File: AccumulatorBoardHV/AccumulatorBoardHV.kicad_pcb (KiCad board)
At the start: 2 copper layers, 179.7 x 69.2 mm, 48 parts, among them J1 TS -> GLV Regulator Jumper, J10 Charger Current, J2 To LV Board, J3 Batt Voltage, J4 TS (Switched), J5 IMD TS, J6 To LV Board, J7 Acc LED 1, J8 Acc LED 2, J9 Charger Current to Batt, U1 V110C12E100BL, U2 DK1A1B-12V, U3 RDD08110S3V3, U4 PS2501-4, U5 G2RL-1A-E, U6 G2RL-1A-E

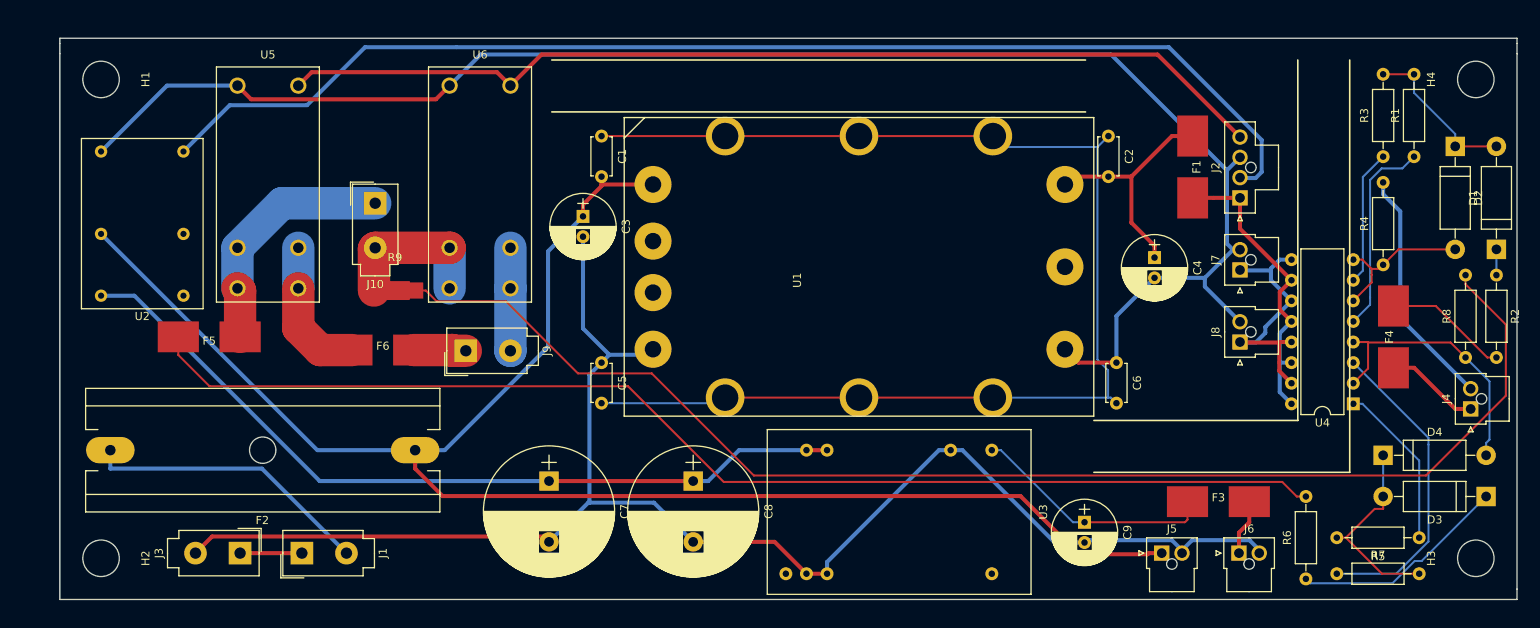
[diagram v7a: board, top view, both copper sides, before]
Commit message: Tweak silkscreen labels on boards for final run
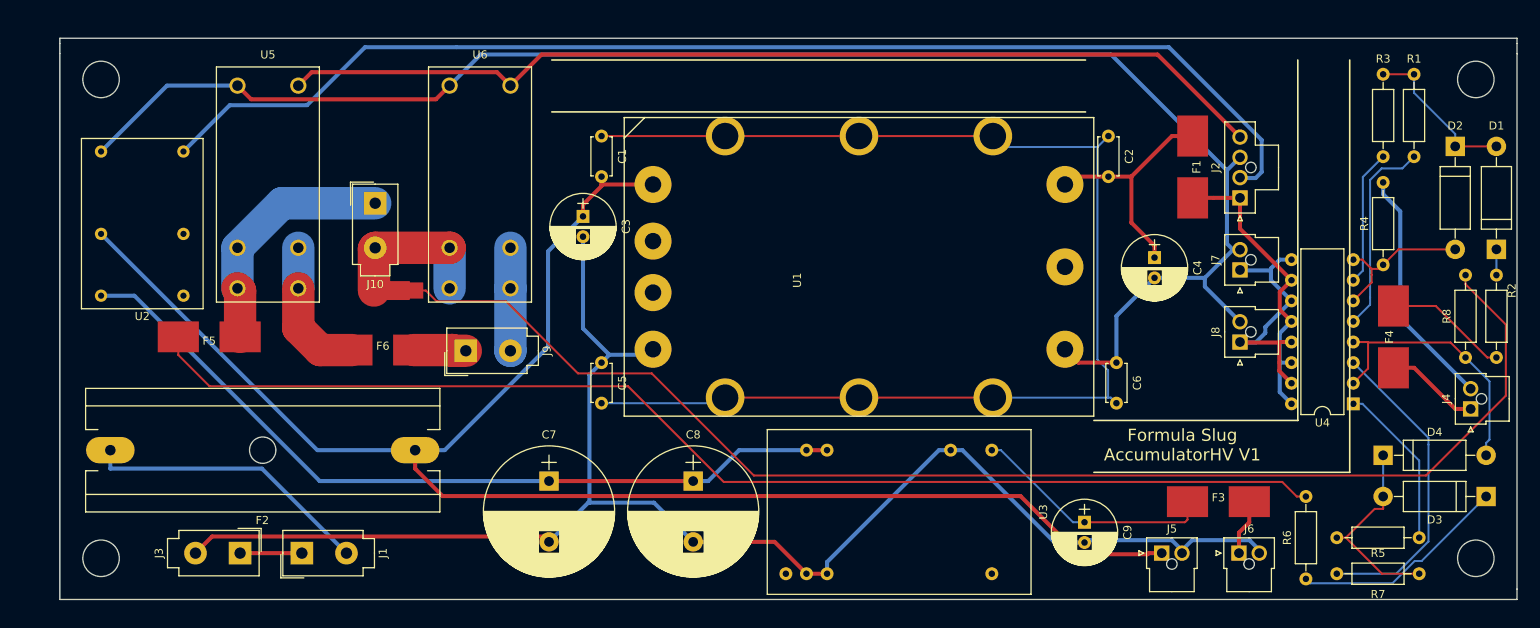
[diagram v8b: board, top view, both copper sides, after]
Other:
- board text added: "Formula Slug AccumulatorHV V1"
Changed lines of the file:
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@@
     (area 21.9 31.019999 204.895 106.253097)
     (thickness 1.6)
-    (drawings 15)
+    (drawings 16)
     (tracks 264)
     (zones 0)
@@
     (descr "Just a \"Net tie\" as an more or less elegant way to connect two different nets without disturbing ERC and DRC.")
     (tags "Just a \"Net tie\" as an more or less elegant way to connect two different nets without disturbing ERC and DRC.")
-    (fp_text reference R9 (at -0.04064 4.06908 180) (layer F.SilkS)
+    (fp_text reference R9 (at 0 -1.905 180) (layer F.SilkS) hide
       (effects (font (size 1 1) (thickness 0.15)))
     )
@@
     (tags "mounting hole 4.5mm no annular")
     (attr virtual)
-    (fp_text reference H4 (at 0 -5.5 90) (layer F.SilkS)
+    (fp_text reference H4 (at 0 -5.5 90) (layer F.SilkS) hide
       (effects (font (size 1 1) (thickness 0.15)))
     )
@@
     (tags "mounting hole 4.5mm no annular")
     (attr virtual)
-    (fp_text reference H3 (at 0 -5.5 90) (layer F.SilkS)
+    (fp_text reference H3 (at 0 -5.5 90) (layer F.SilkS) hide
       (effects (font (size 1 1) (thickness 0.15)))
     )
@@
     (tags "mounting hole 4.5mm no annular")
     (attr virtual)
-    (fp_text reference H2 (at 0 -5.5 270) (layer F.SilkS)
+    (fp_text reference H2 (at 0 -5.5 270) (layer F.SilkS) hide
       (effects (font (size 1 1) (thickness 0.15)))
     )
@@
     (tags "mounting hole 4.5mm no annular")
     (attr virtual)
-    (fp_text reference H1 (at 0 -5.5 270) (layer F.SilkS)
+    (fp_text reference H1 (at 0 -5.5 270) (layer F.SilkS) hide
       (effects (font (size 1 1) (thickness 0.15)))
     )
@@
     (descr "CP, Radial series, Radial, pin pitch=7.50mm, , diameter=16mm, Electrolytic Capacitor")
     (tags "CP Radial series Radial pin pitch 7.50mm  diameter 16mm Electrolytic Capacitor")
-    (fp_text reference C7 (at 3.75 -9.31 270) (layer F.SilkS)
+    (fp_text reference C7 (at -5.715 0 360) (layer F.SilkS)
       (effects (font (size 1 1) (thickness 0.15)))
     )
@@
     (descr "CP, Radial series, Radial, pin pitch=7.50mm, , diameter=16mm, Electrolytic Capacitor")
     (tags "CP Radial series Radial pin pitch 7.50mm  diameter 16mm Electrolytic Capacitor")
-    (fp_text reference C8 (at 3.75 -9.31 270) (layer F.SilkS)
+    (fp_text reference C8 (at -5.715 0 360) (layer F.SilkS)
       (effects (font (size 1 1) (thickness 0.15)))
     )
@@
     (descr "D, DO-15 series, Axial, Horizontal, pin pitch=12.7mm, , length*diameter=7.6*3.6mm^2, , http://www.diodes.com/_files/packages/DO-15.pdf")
     (tags "D DO-15 series Axial Horizontal pin pitch 12.7mm  length 7.6mm diameter 3.6mm")
-    (fp_text reference D1 (at 6.35 -2.86 90) (layer F.SilkS)
+    (fp_text reference D1 (at 15.24 0 180) (layer F.SilkS)
       (effects (font (size 1 1) (thickness 0.15)))
     )
@@
     (descr "D, DO-15 series, Axial, Horizontal, pin pitch=12.7mm, , length*diameter=7.6*3.6mm^2, , http://www.diodes.com/_files/packages/DO-15.pdf")
     (tags "D DO-15 series Axial Horizontal pin pitch 12.7mm  length 7.6mm diameter 3.6mm")
-    (fp_text reference D2 (at 6.35 -2.86 270) (layer F.SilkS)
+    (fp_text reference D2 (at -2.54 0 360) (layer F.SilkS)
       (effects (font (size 1 1) (thickness 0.15)))
     )
@@
     (descr "Resistor, Axial_DIN0207 series, Axial, Horizontal, pin pitch=10.16mm, 0.25W = 1/4W, length*diameter=6.3*2.5mm^2, http://cdn-reichelt.de/documents/datenblatt/B400/1_4W%23YAG.pdf")
     (tags "Resistor Axial_DIN0207 series Axial Horizontal pin pitch 10.16mm 0.25W = 1/4W length 6.3mm diameter 2.5mm")
-    (fp_text reference R1 (at 5.08 -2.31 90) (layer F.SilkS)
+    (fp_text reference R1 (at 12.065 0 180) (layer F.SilkS)
       (effects (font (size 1 1) (thickness 0.15)))
     )
@@
     (descr "Resistor, Axial_DIN0207 series, Axial, Horizontal, pin pitch=10.16mm, 0.25W = 1/4W, length*diameter=6.3*2.5mm^2, http://cdn-reichelt.de/documents/datenblatt/B400/1_4W%23YAG.pdf")
     (tags "Resistor Axial_DIN0207 series Axial Horizontal pin pitch 10.16mm 0.25W = 1/4W length 6.3mm diameter 2.5mm")
-    (fp_text reference R2 (at 5.08 -2.31 270) (layer F.SilkS)
+    (fp_text reference R2 (at 1.905 -1.905 270) (layer F.SilkS)
       (effects (font (size 1 1) (thickness 0.15)))
     )
@@
     (descr "Resistor, Axial_DIN0207 series, Axial, Horizontal, pin pitch=10.16mm, 0.25W = 1/4W, length*diameter=6.3*2.5mm^2, http://cdn-reichelt.de/documents/datenblatt/B400/1_4W%23YAG.pdf")
     (tags "Resistor Axial_DIN0207 series Axial Horizontal pin pitch 10.16mm 0.25W = 1/4W length 6.3mm diameter 2.5mm")
-    (fp_text reference R3 (at 5.08 -2.31 90) (layer F.SilkS)
+    (fp_text reference R3 (at 12.065 0 180) (layer F.SilkS)
       (effects (font (size 1 1) (thickness 0.15)))
     )
@@
     (descr "Resistor, Axial_DIN0207 series, Axial, Horizontal, pin pitch=10.16mm, 0.25W = 1/4W, length*diameter=6.3*2.5mm^2, http://cdn-reichelt.de/documents/datenblatt/B400/1_4W%23YAG.pdf")
     (tags "Resistor Axial_DIN0207 series Axial Horizontal pin pitch 10.16mm 0.25W = 1/4W length 6.3mm diameter 2.5mm")
-    (fp_text reference R5 (at 5.08 -2.31 180) (layer F.SilkS)
+    (fp_text reference R5 (at 5.08 -1.905 180) (layer F.SilkS)
       (effects (font (size 1 1) (thickness 0.15)))
     )
@@
     (descr "Resistor, Axial_DIN0207 series, Axial, Horizontal, pin pitch=10.16mm, 0.25W = 1/4W, length*diameter=6.3*2.5mm^2, http://cdn-reichelt.de/documents/datenblatt/B400/1_4W%23YAG.pdf")
     (tags "Resistor Axial_DIN0207 series Axial Horizontal pin pitch 10.16mm 0.25W = 1/4W length 6.3mm diameter 2.5mm")
-    (fp_text reference R7 (at 5.08 -2.31) (layer F.SilkS)
+    (fp_text reference R7 (at 5.08 2.54) (layer F.SilkS)
       (effects (font (size 1 1) (thickness 0.15)))
     )
@@
       (net 19 /AIRS_FINAL_CHARGER))
   )
+  (gr_text "Formula Slug\nAccumulatorHV V1" (at 161.925 81.28) (layer F.SilkS)
+    (effects (font (size 1.5 1.5) (thickness 0.3)))
+  )
   (gr_line (start 203.2 31.115) (end 203.2 31.75) (angle 90) (layer Edge.Cuts) (width 0.1))
   (gr_line (start 23.495 31.115) (end 203.2 31.115) (angle 90) (layer Edge.Cuts) (width 0.1))
@@
   (segment (start 190.5 35.56) (end 186.69 35.56) (width 0.25) (layer F.Cu) (net 8))
   (segment (start 185.2697 60.2936) (end 185.2697 61.2373) (width 0.25) (layer F.Cu) (net 9))
-  (segment (start 185.2697 61.2373) (end 183.007 63.5) (width 0.25) (layer F.Cu) (net 9) (status 800000))
+  (segment (start 185.2697 61.2373) (end 183.007 63.5) (width 0.25) (layer F.Cu) (net 9))
   (segment (start 188.595 57.15) (end 186.69 59.055) (width 0.25) (layer F.Cu) (net 9))
   (segment (start 195.58 57.15) (end 188.595 57.15) (width 0.25) (layer F.Cu) (net 9))
@@
   (segment (start 185.2697 59.5574) (end 184.1323 58.42) (width 0.25) (layer F.Cu) (net 9))
   (segment (start 190.5839 95.5879) (end 191.4321 95.5879) (width 0.25) (layer B.Cu) (net 10))
-  (segment (start 191.4321 95.5879) (end 199.39 87.63) (width 0.25) (layer B.Cu) (net 10) (status 800000))
+  (segment (start 191.4321 95.5879) (end 199.39 87.63) (width 0.25) (layer B.Cu) (net 10))
   (segment (start 177.7069 98.3319) (end 177.165 97.79) (width 0.25) (layer B.Cu) (net 10))
   (segment (start 187.8399 98.3319) (end 177.7069 98.3319) (width 0.25) (layer B.Cu) (net 10))
@@
   (segment (start 186.69 87.63) (end 186.69 89.1553) (width 0.25) (layer F.Cu) (net 11))
   (segment (start 184.831 70.992) (end 184.831 71.836) (width 0.25) (layer F.Cu) (net 12))
-  (segment (start 184.831 71.836) (end 183.007 73.66) (width 0.25) (layer F.Cu) (net 12) (status 800000))
+  (segment (start 184.831 71.836) (end 183.007 73.66) (width 0.25) (layer F.Cu) (net 12))
   (segment (start 199.8048 73.4398) (end 196.85 70.485) (width 0.25) (layer B.Cu) (net 12))
   (segment (start 199.8048 80.6099) (end 199.8048 73.4398) (width 0.25) (layer B.Cu) (net 12))
@@
   (segment (start 71.561 56.957) (end 71.561 61.957) (width 4) (layer B.Cu) (net 22))
   (segment (start 185.0785 63.1245) (end 185.0785 63.9685) (width 0.25) (layer B.Cu) (net 23))
-  (segment (start 185.0785 63.9685) (end 183.007 66.04) (width 0.25) (layer B.Cu) (net 23) (status 800000))
+  (segment (start 185.0785 63.9685) (end 183.007 66.04) (width 0.25) (layer B.Cu) (net 23))
   (segment (start 185.0785 48.5938) (end 185.0785 63.1245) (width 0.25) (layer B.Cu) (net 23))
   (segment (start 186.5063 47.166) (end 185.0785 48.5938) (width 0.25) (layer B.Cu) (net 23))
@@
   (segment (start 190.5 45.72) (end 189.054 47.166) (width 0.25) (layer B.Cu) (net 23))
   (segment (start 184.1873 58.8313) (end 184.1873 59.7797) (width 0.25) (layer B.Cu) (net 24))
-  (segment (start 184.1873 59.7797) (end 183.007 60.96) (width 0.25) (layer B.Cu) (net 24) (status 800000))
+  (segment (start 184.1873 59.7797) (end 183.007 60.96) (width 0.25) (layer B.Cu) (net 24))
   (segment (start 184.1873 48.2227) (end 184.1873 58.8313) (width 0.25) (layer B.Cu) (net 24))
   (segment (start 186.69 45.72) (end 184.1873 48.2227) (width 0.25) (layer B.Cu) (net 24))
@@
   (segment (start 183.007 76.2) (end 184.1323 76.2) (width 0.25) (layer B.Cu) (net 25))
   (segment (start 192.2799 81.2369) (end 192.2799 80.3929) (width 0.25) (layer B.Cu) (net 26))
-  (segment (start 192.2799 80.3929) (end 183.007 71.12) (width 0.25) (layer B.Cu) (net 26) (status 800000))
+  (segment (start 192.2799 80.3929) (end 183.007 71.12) (width 0.25) (layer B.Cu) (net 26))
   (segment (start 192.2799 93.1816) (end 192.2799 81.2369) (width 0.25) (layer B.Cu) (net 26))
   (segment (start 188.3065 97.155) (end 192.2799 93.1816) (width 0.25) (layer B.Cu) (net 26))
